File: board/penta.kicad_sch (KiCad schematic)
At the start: 141 parts, among them J1 USB_C_Receptacle_PowerOnly_6P, U1 XIAO-RP2040-SMD

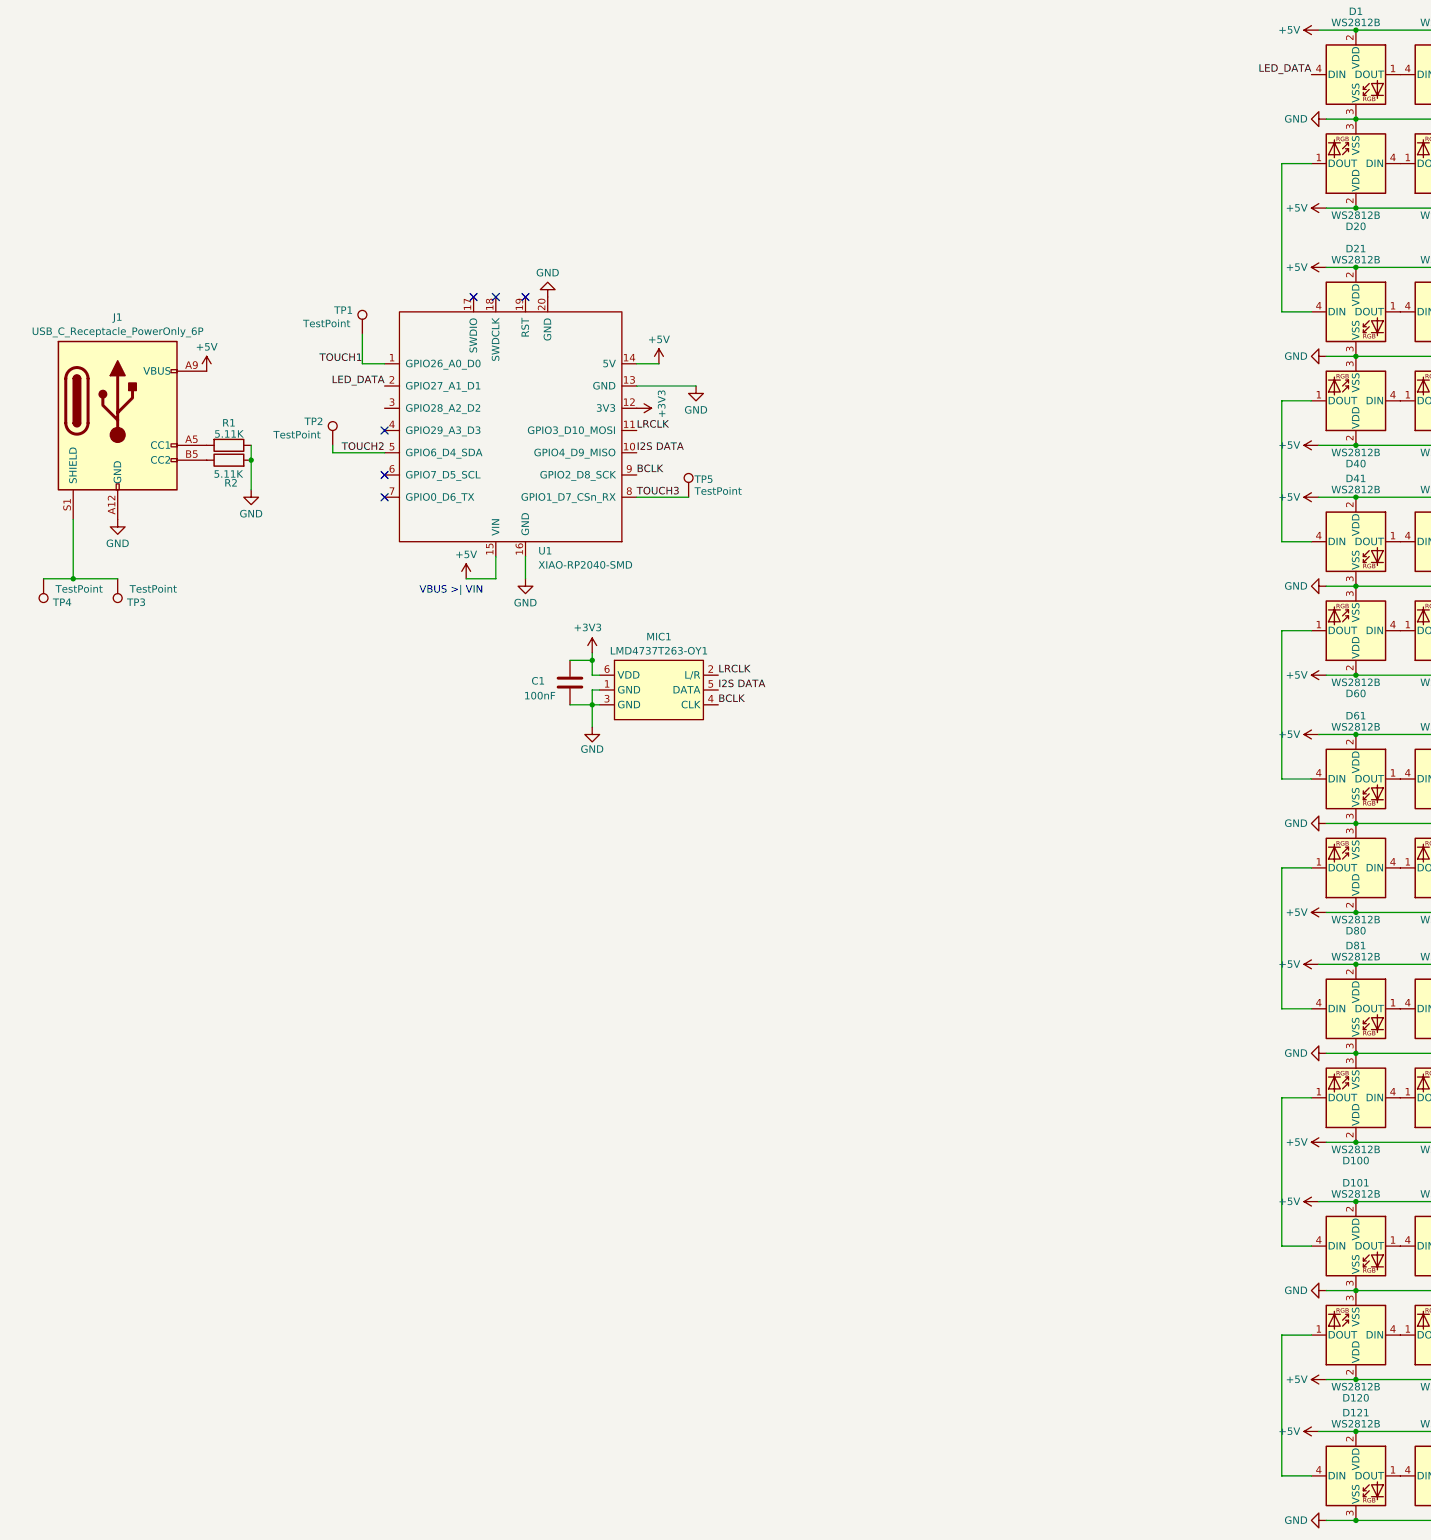
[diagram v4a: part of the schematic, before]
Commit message: add an nfet so we can power down pixels for whatever saves that'll get doing larger pattern work; make 4-layer board to support switching a gnd plane off; decorate
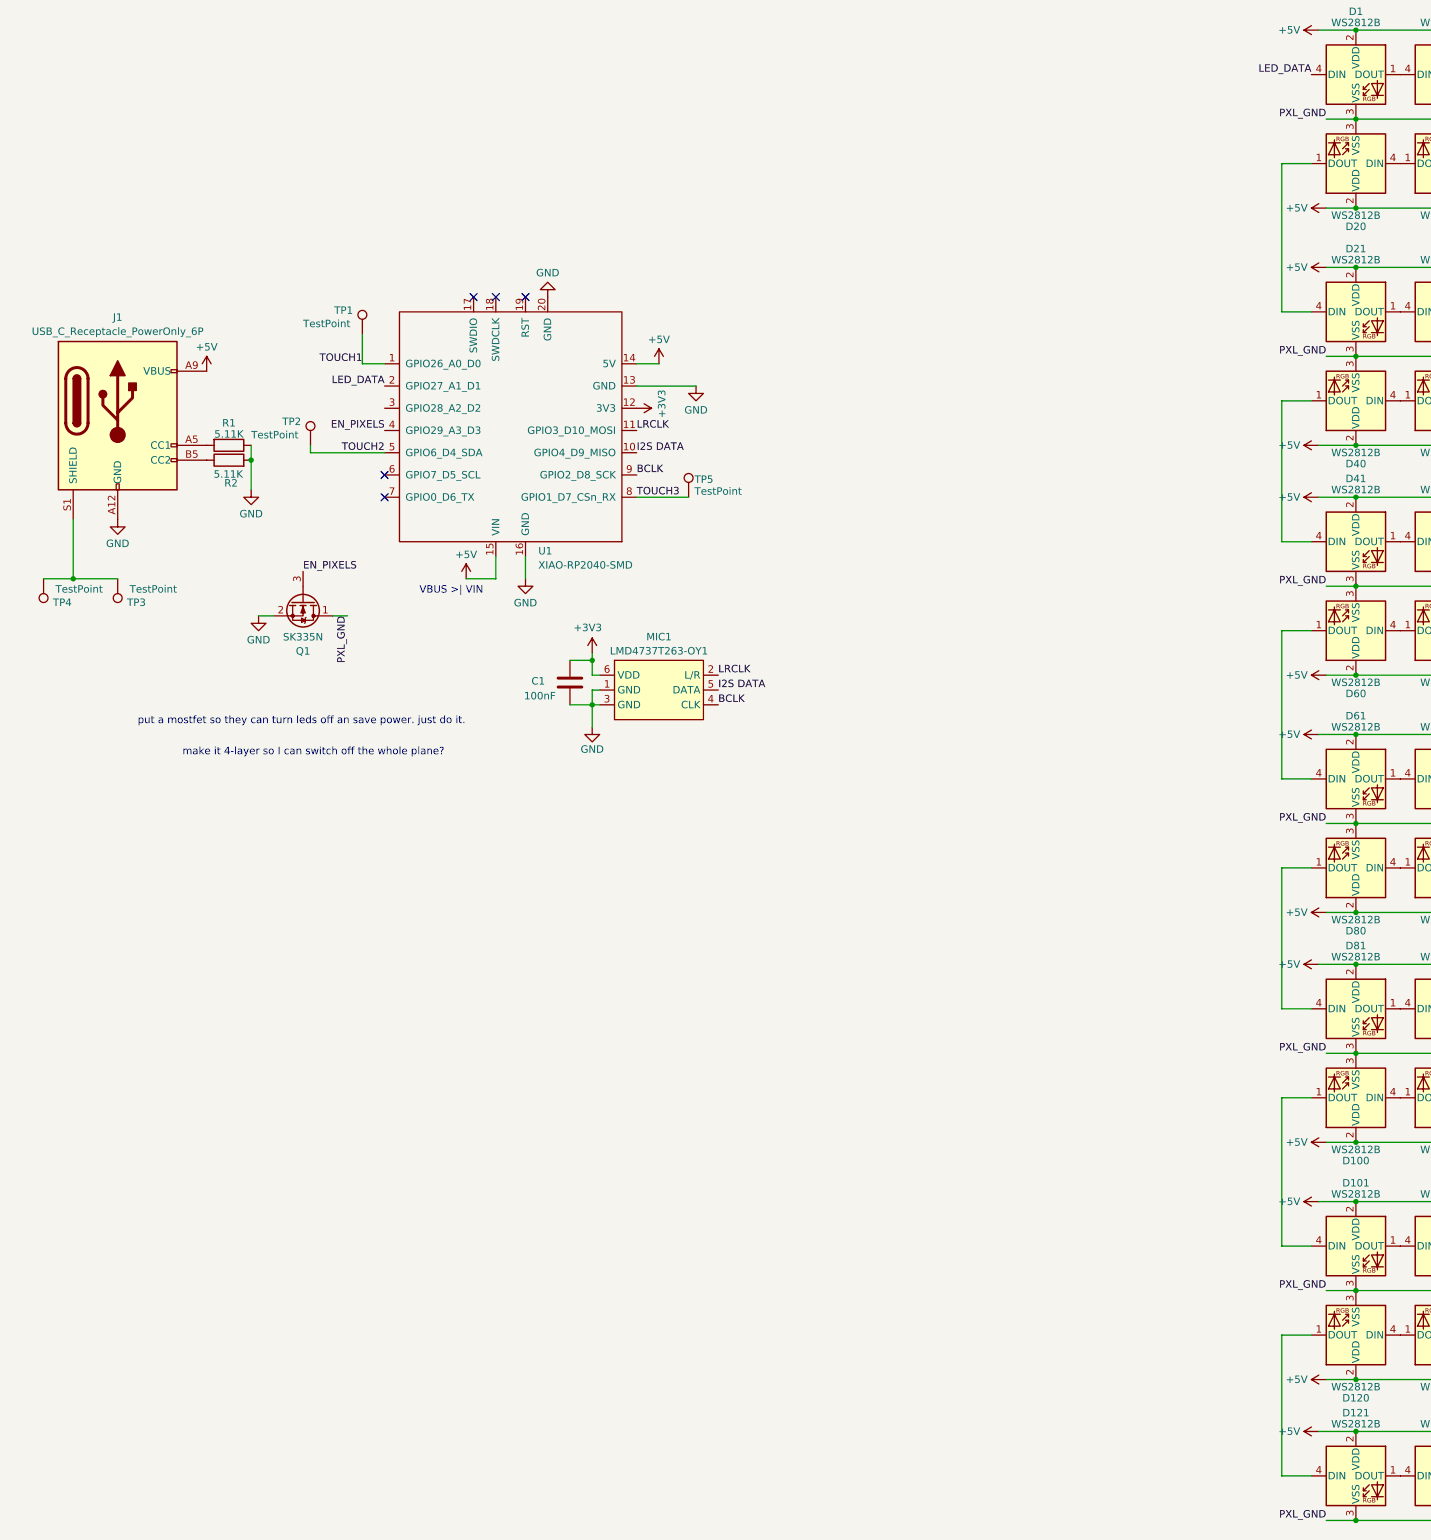
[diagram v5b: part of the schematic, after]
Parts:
- added Q1: SK335N, Package_TO_SOT_SMD:SOT-23, symbol Device:Q_NMOS_DSG
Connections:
- net GND: now also Q1.2 (S); no longer D1.3 (VSS), D10.3 (VSS), D100.3 (VSS), D101.3 (VSS), D102.3 (VSS), D103.3 (VSS), D104.3 (VSS), D105.3 (VSS), D106.3 (VSS), D107.3 (VSS), D108.3 (VSS), D109.3 (VSS), D11.3 (VSS), D110.3 (VSS), D111.3 (VSS), D112.3 (VSS), D113.3 (VSS), D114.3 (VSS), D115.3 (VSS), D116.3 (VSS), D117.3 (VSS), D118.3 (VSS), D119.3 (VSS), D12.3 (VSS), D120.3 (VSS), D121.3 (VSS), D122.3 (VSS), D123.3 (VSS), D124.3 (VSS), D125.3 (VSS), D13.3 (VSS), D14.3 (VSS), D15.3 (VSS), D16.3 (VSS), D17.3 (VSS), D18.3 (VSS), D19.3 (VSS), D2.3 (VSS), D20.3 (VSS), D21.3 (VSS), D22.3 (VSS), D23.3 (VSS), D24.3 (VSS), D25.3 (VSS), D26.3 (VSS), D27.3 (VSS), D28.3 (VSS), D29.3 (VSS), D3.3 (VSS), D30.3 (VSS), D31.3 (VSS), D32.3 (VSS), D33.3 (VSS), D34.3 (VSS), D35.3 (VSS), D36.3 (VSS), D37.3 (VSS), D38.3 (VSS), D39.3 (VSS), D4.3 (VSS), D40.3 (VSS), D41.3 (VSS), D42.3 (VSS), D43.3 (VSS), D44.3 (VSS), D45.3 (VSS), D46.3 (VSS), D47.3 (VSS), D48.3 (VSS), D49.3 (VSS), D5.3 (VSS), D50.3 (VSS), D51.3 (VSS), D52.3 (VSS), D53.3 (VSS), D54.3 (VSS), D55.3 (VSS), D56.3 (VSS), D57.3 (VSS), D58.3 (VSS), D59.3 (VSS), D6.3 (VSS), D60.3 (VSS), D61.3 (VSS), D62.3 (VSS), D63.3 (VSS), D64.3 (VSS), D65.3 (VSS), D66.3 (VSS), D67.3 (VSS), D68.3 (VSS), D69.3 (VSS), D7.3 (VSS), D70.3 (VSS), D71.3 (VSS), D72.3 (VSS), D73.3 (VSS), D74.3 (VSS), D75.3 (VSS), D76.3 (VSS), D77.3 (VSS), D78.3 (VSS), D79.3 (VSS), D8.3 (VSS), D80.3 (VSS), D81.3 (VSS), D82.3 (VSS), D83.3 (VSS), D84.3 (VSS), D85.3 (VSS), D86.3 (VSS), D87.3 (VSS), D88.3 (VSS), D89.3 (VSS), D9.3 (VSS), D90.3 (VSS), D91.3 (VSS), D92.3 (VSS), D93.3 (VSS), D94.3 (VSS), D95.3 (VSS), D96.3 (VSS), D97.3 (VSS), D98.3 (VSS), D99.3 (VSS)
- net EN_PIXELS: now reaches U1.4 (GPIO29_A3_D3)
- net EN_PIXELS: now also Q1.3 (G)
- new net PXL_GND: D1.3 (VSS), D10.3 (VSS), D100.3 (VSS), D101.3 (VSS), D102.3 (VSS), D103.3 (VSS), D104.3 (VSS), D105.3 (VSS), D106.3 (VSS), D107.3 (VSS), D108.3 (VSS), D109.3 (VSS), D11.3 (VSS), D110.3 (VSS), D111.3 (VSS), D112.3 (VSS), D113.3 (VSS), D114.3 (VSS), D115.3 (VSS), D116.3 (VSS), D117.3 (VSS), D118.3 (VSS), D119.3 (VSS), D12.3 (VSS), D120.3 (VSS), D121.3 (VSS), D122.3 (VSS), D123.3 (VSS), D124.3 (VSS), D125.3 (VSS), D13.3 (VSS), D14.3 (VSS), D15.3 (VSS), D16.3 (VSS), D17.3 (VSS), D18.3 (VSS), D19.3 (VSS), D2.3 (VSS), D20.3 (VSS), D21.3 (VSS), D22.3 (VSS), D23.3 (VSS), D24.3 (VSS), D25.3 (VSS), D26.3 (VSS), D27.3 (VSS), D28.3 (VSS), D29.3 (VSS), D3.3 (VSS), D30.3 (VSS), D31.3 (VSS), D32.3 (VSS), D33.3 (VSS), D34.3 (VSS), D35.3 (VSS), D36.3 (VSS), D37.3 (VSS), D38.3 (VSS), D39.3 (VSS), D4.3 (VSS), D40.3 (VSS), D41.3 (VSS), D42.3 (VSS), D43.3 (VSS), D44.3 (VSS), D45.3 (VSS), D46.3 (VSS), D47.3 (VSS), D48.3 (VSS), D49.3 (VSS), D5.3 (VSS), D50.3 (VSS), D51.3 (VSS), D52.3 (VSS), D53.3 (VSS), D54.3 (VSS), D55.3 (VSS), D56.3 (VSS), D57.3 (VSS), D58.3 (VSS), D59.3 (VSS), D6.3 (VSS), D60.3 (VSS), D61.3 (VSS), D62.3 (VSS), D63.3 (VSS), D64.3 (VSS), D65.3 (VSS), D66.3 (VSS), D67.3 (VSS), D68.3 (VSS), D69.3 (VSS), D7.3 (VSS), D70.3 (VSS), D71.3 (VSS), D72.3 (VSS), D73.3 (VSS), D74.3 (VSS), D75.3 (VSS), D76.3 (VSS), D77.3 (VSS), D78.3 (VSS), D79.3 (VSS), D8.3 (VSS), D80.3 (VSS), D81.3 (VSS), D82.3 (VSS), D83.3 (VSS), D84.3 (VSS), D85.3 (VSS), D86.3 (VSS), D87.3 (VSS), D88.3 (VSS), D89.3 (VSS), D9.3 (VSS), D90.3 (VSS), D91.3 (VSS), D92.3 (VSS), D93.3 (VSS), D94.3 (VSS), D95.3 (VSS), D96.3 (VSS), D97.3 (VSS), D98.3 (VSS), D99.3 (VSS), Q1.1 (D)
- no-connect marks 7 -> 6
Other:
- note added: "make it 4-layer so I can switch off the whole plane?"
- note added: "put a mostfet so they can turn leds off an save power. just do it."
- moved on the sheet: TP2

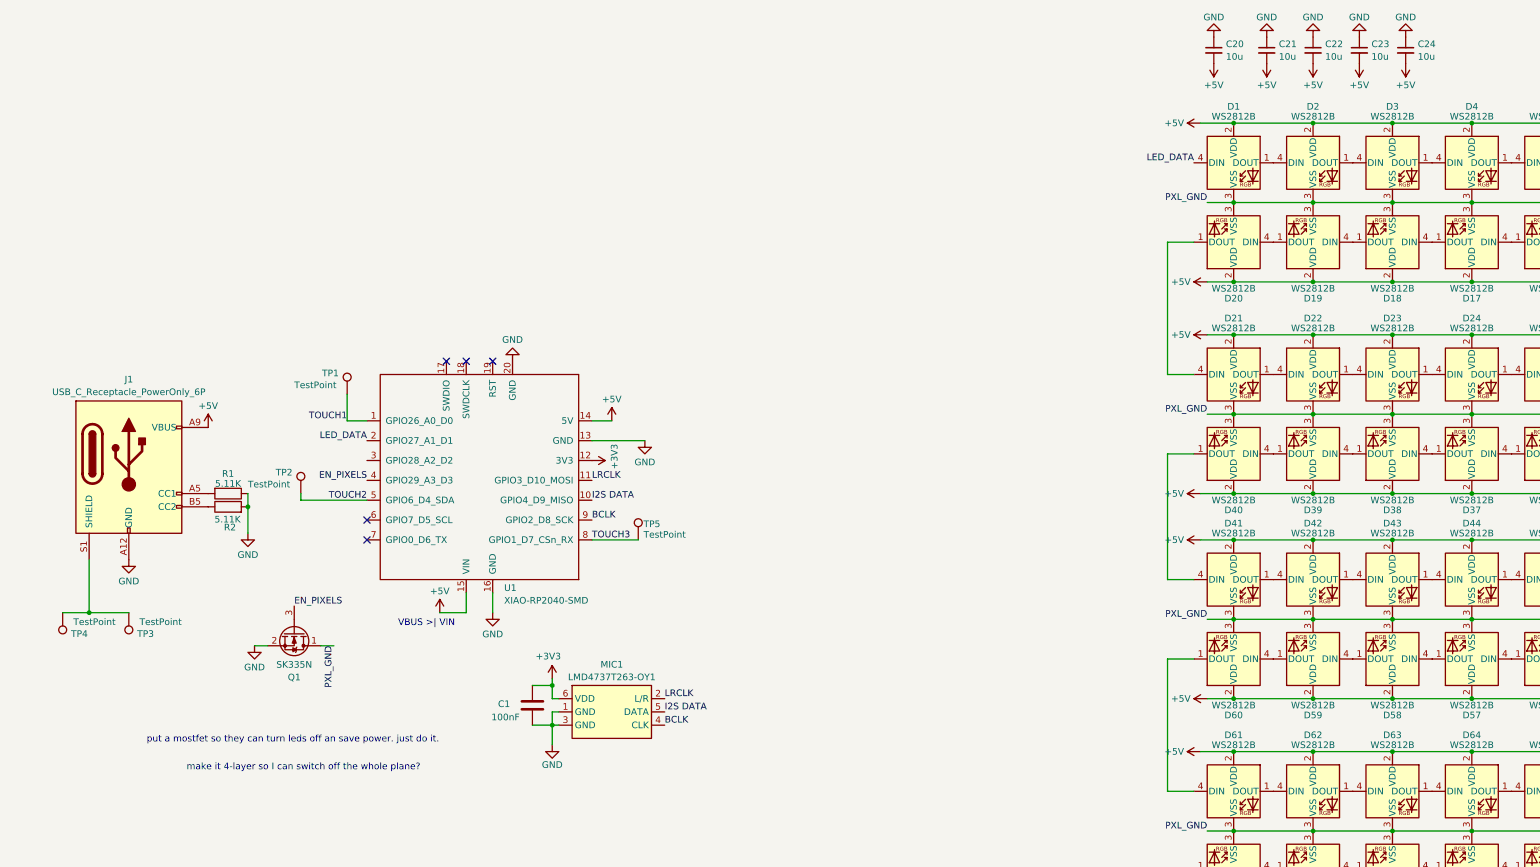
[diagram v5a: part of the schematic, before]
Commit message: pins rearrangement to make touch pads work; minor fixes and polish
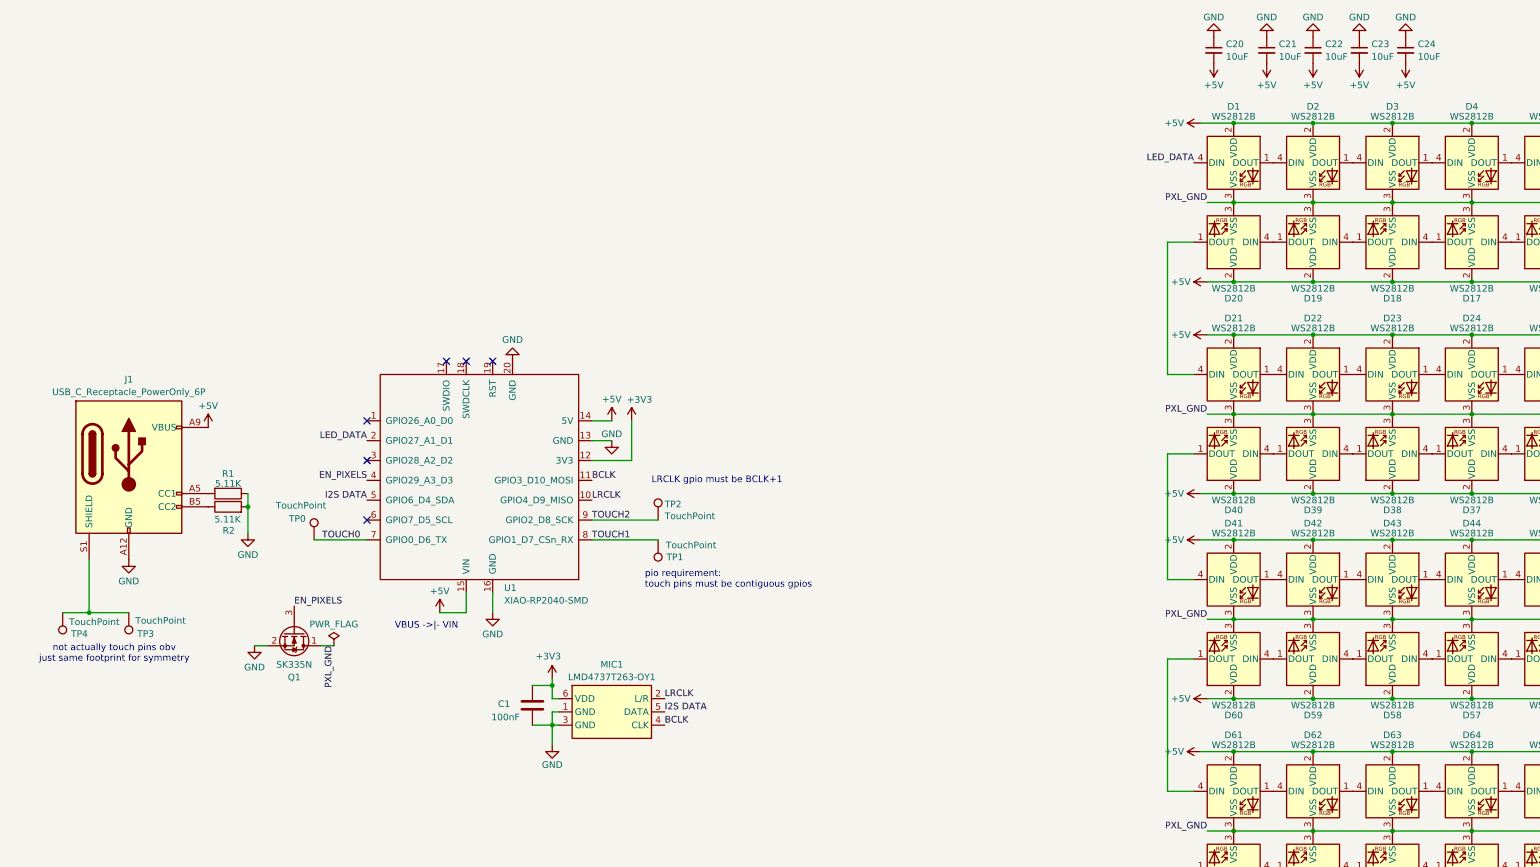
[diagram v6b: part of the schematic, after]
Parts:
- C20, C21, C22, C23, C24: value 10u -> 10uF
- TP0: renamed from TP2; value TestPoint -> TouchPoint
- TP1: renamed from TP5; value TestPoint -> TouchPoint
- TP2: renamed from TP1; value TestPoint -> TouchPoint
- TP3, TP4: value TestPoint -> TouchPoint
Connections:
- net TOUCH3 is gone; now on net TOUCH1: TP1.1, U1.8 (GPIO1_D7_CSn_RX)
- net BCLK: now also U1.11 (GPIO3_D10_MOSI); no longer U1.9 (GPIO2_D8_SCK)
- net I2S DATA: now also U1.5 (GPIO6_D4_SDA); no longer U1.10 (GPIO4_D9_MISO)
- net LRCLK: now also U1.10 (GPIO4_D9_MISO); no longer U1.11 (GPIO3_D10_MOSI)
- net TOUCH1: no longer TP2.1, U1.1 (GPIO26_A0_D0)
- net TOUCH2: now also TP2.1, U1.9 (GPIO2_D8_SCK); no longer TP0.1, U1.5 (GPIO6_D4_SDA)
- net TOUCH0: now reaches U1.7 (GPIO0_D6_TX)
- net TOUCH0: now also TP0.1
- no-connect marks 6 -> 7
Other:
- note added: "LRCLK gpio must be BCLK+1"
- note added: "VBUS ->|- VIN"
- note added: "not actually touch pins obv just same footprint for symmetry"
- note added: "pio requirement: touch pins must be contiguous gpios"
- note removed: "VBUS >| VIN"
- note removed: "make it 4-layer so I can switch off the whole plane?"
- note removed: "put a mostfet so they can turn leds off an save power. just do it."
- moved on the sheet: TP0, TP1, TP2

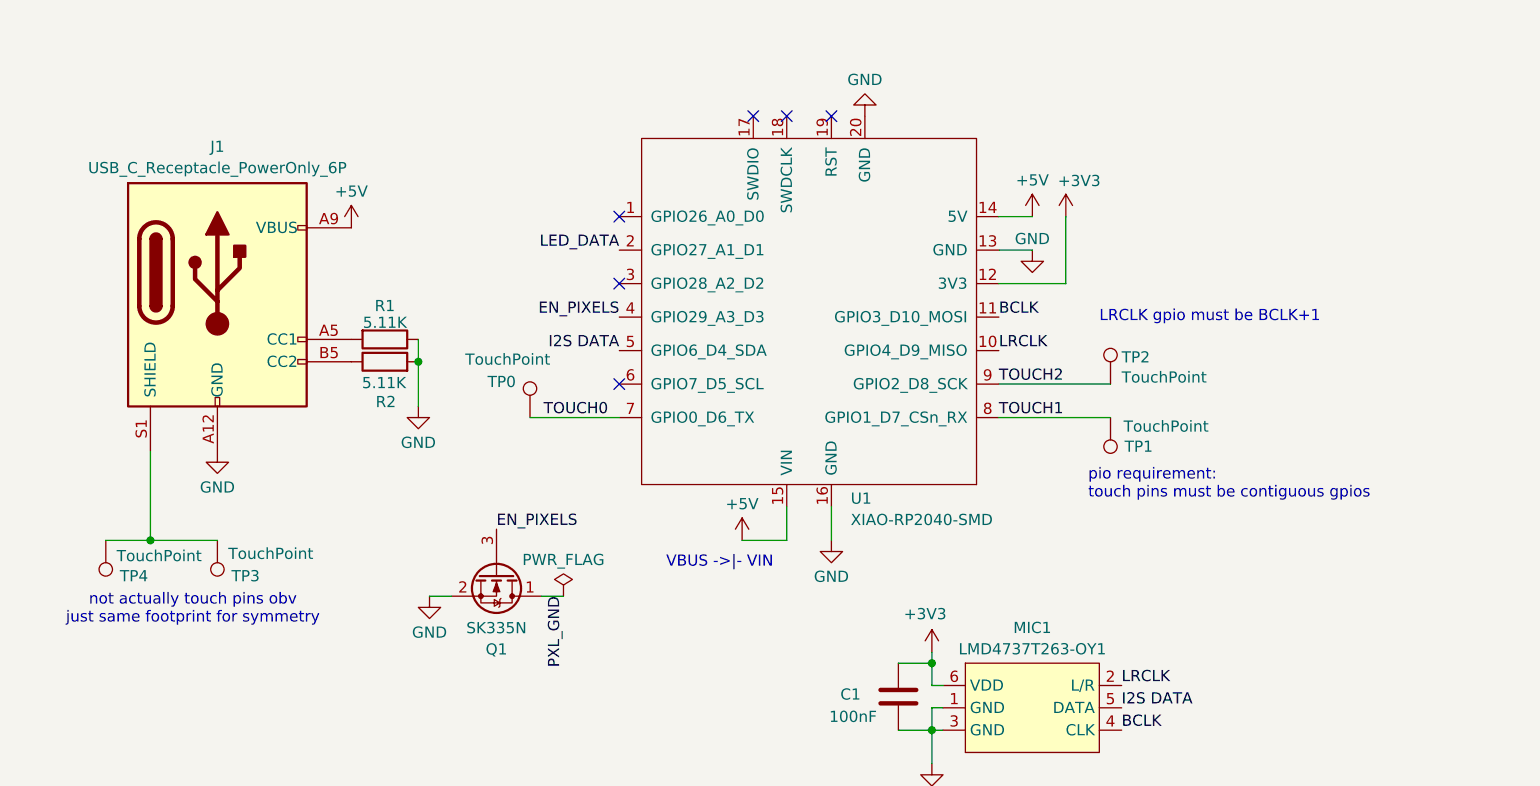
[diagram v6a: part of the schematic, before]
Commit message: ok. support all 5 touch pins because we can
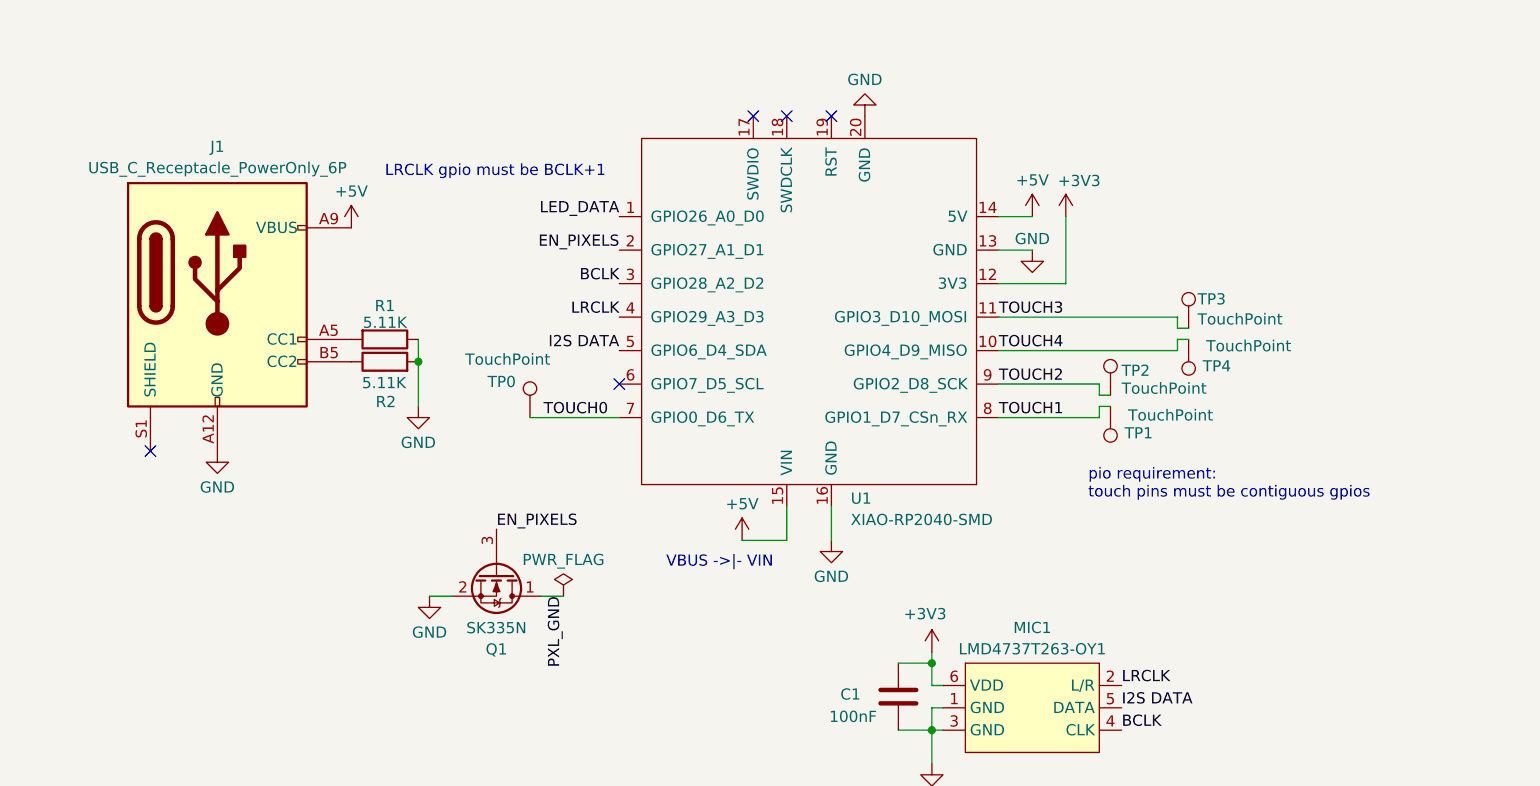
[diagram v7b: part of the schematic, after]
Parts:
- MIC1: footprint easyeda2kicad:LGA-6_L4.7-W3.8-P1.65_LMD4737T -> penta:LGA-6_L4.7-W3.8-P1.65_LMD4737T
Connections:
- net BCLK: now also U1.3 (GPIO28_A2_D2); no longer U1.11 (GPIO3_D10_MOSI)
- net EN_PIXELS: now also U1.2 (GPIO27_A1_D1); no longer U1.4 (GPIO29_A3_D3)
- net LED_DATA: now also U1.1 (GPIO26_A0_D0); no longer U1.2 (GPIO27_A1_D1)
- net LRCLK: now also U1.4 (GPIO29_A3_D3); no longer U1.10 (GPIO4_D9_MISO)
- new net TOUCH3: TP3.1, U1.11 (GPIO3_D10_MOSI)
- new net TOUCH4: TP4.1, U1.10 (GPIO4_D9_MISO)
- now unconnected: J1.S1 (SHIELD)
- no-connect marks 7 -> 6
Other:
- note removed: "not actually touch pins obv just same footprint for symmetry"
- moved on the sheet: TP1, TP2, TP3, TP4
